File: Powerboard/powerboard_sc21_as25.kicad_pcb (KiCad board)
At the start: 2 copper layers, 86.2 x 40 mm, 117 parts, among them IC1 BQ24618RGET-iclr, IC2 CP2102, Q1 SI7617DN-T1-GE3, Q10 CSD25302Q2, Q2 SI7617DN-T1-GE3, Q3 SI7617DN-T1-GE3, Q6 MMDT2222A, Q7 SI7617DN-T1-GE3, Q8 SI7617DN-T1-GE3, Q9 CSD25302Q2, U1 LTC4412xS6, U10 RT9025-25GSP, U11 LTC4411, U2 ESP32-PICO-D4, U3 SN65HVD230, U4 LTC4412xS6, U5 LTC4412xS6, U6 LM2679T-3.3-iclr, U7 LM2679T-3.3-iclr, U8 LTC4412xS6, U9 LTC4412xS6

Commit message: changed some FP assignments and imported components
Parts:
- removed ANT1: AMCA31-2R450G-S1F-T3, iclr:ANT_AMCA31-2R450G-S1F-T3
- removed R25: 3.5k, Resistor_SMD:R_0603_1608Metric
- removed R33: 24k, Resistor_SMD:R_0603_1608Metric
- removed R34: 47k, Resistor_SMD:R_0603_1608Metric
- removed REF** (x2): AMASS_XT60-M, AMASS_XT60-M
- removed REF** (x4): MountingHole_3.2mm_M3_DIN965_Pad, MountingHole:MountingHole_3.2mm_M3_DIN965_Pad
- removed REF**: USB_C_Receptacle_GCT_USB4085, Connector_USB:USB_C_Receptacle_GCT_USB4085
- removed REF**: Molex_Mini-Fit_Jr_5566-08A_2x04_P4.20mm_Vertical, Connector_Molex:Molex_Mini-Fit_Jr_5566-08A_2x04_P4.20mm_Vertical
- removed REF**: Molex_Mini-Fit_Jr_5566-04A_2x02_P4.20mm_Vertical, Connector_Molex:Molex_Mini-Fit_Jr_5566-04A_2x02_P4.20mm_Vertical
- removed U4, U5: LTC4412xS6, Package_TO_SOT_SMD:TSOT-23-6
- added C26: 0.1uF, Capacitor_SMD:C_0603_1608Metric, F.Cu at (229.3, 118.8)
- added C27: 220pF, Capacitor_SMD:C_0603_1608Metric, F.Cu at (233.3, 119.9)
- added C28: 220 pF, Capacitor_SMD:C_0603_1608Metric, F.Cu at (266.8, 84.4)
- added C29: 15uF, Capacitor_SMD:CP_Elec_5x5.3, F.Cu at (240.5, 62.0)
- added C30: 15uF, Capacitor_SMD:CP_Elec_5x5.3, F.Cu at (260.4, 56.0)
- added C31: 0.1μF, Capacitor_SMD:C_0603_1608Metric, F.Cu at (330.1, 51.2)
- added C32: 22μF, Capacitor_SMD:C_1210_3225Metric, F.Cu at (282.3, 73.2)
- added C33: 0.1μF, Capacitor_SMD:C_0603_1608Metric, F.Cu at (334.6, 44.8)
- added C36: 0.01uF, Capacitor_SMD:C_0603_1608Metric, F.Cu at (263.6, 41.4)
- added C37: 0.01uF, Capacitor_SMD:C_0603_1608Metric, F.Cu at (226.8, 76.9)
- added C38: 330uF, Capacitor_SMD:CP_Elec_10x10, F.Cu at (243.3, 39.2)
- added C39: 330uF, Capacitor_SMD:CP_Elec_10x10, F.Cu at (215.2, 37.0)
- added C51: 0.1muF, Capacitor_SMD:C_0603_1608Metric, F.Cu at (288.8, 100.2)
- added C52: 4.7muF, Capacitor_SMD:C_0603_1608Metric, F.Cu at (293.2, 97.0)
- added C53: 0.1muF, Capacitor_SMD:C_0603_1608Metric, F.Cu at (302.6, 87.4)
- added C54: 10uF, Capacitor_SMD:C_0805_2012Metric, F.Cu at (298.8, 84.7)
- added C57: 10uF, Capacitor_SMD:C_0805_2012Metric, F.Cu at (291.4, 91.8)
- added C58: 4.7uF, Capacitor_SMD:C_0603_1608Metric, F.Cu at (284.7, 102.1)
- added D1: BAT54, Diode_SMD:D_SOT-23_ANK, F.Cu at (344.0, 35.6)
- added D4: SM712_SOT23, Package_TO_SOT_SMD:SOT-23, F.Cu at (222.2, 123.7)
- added D5: DST1550S, Package_TO_SOT_SMD:TO-277B, F.Cu at (250.3, 58.0)
- added D8: SP0503BAHT, Package_TO_SOT_SMD:SOT-143, F.Cu at (288.6, 96.7)
- added H1: MountingHole_Pad, MountingHole:MountingHole_3.2mm_M3_DIN965_Pad, F.Cu at (210.6, 122.4)
- added H2: MountingHole_Pad, MountingHole:MountingHole_3.2mm_M3_DIN965_Pad, F.Cu at (261.2, 86.8)
- added H3: MountingHole_Pad, MountingHole:MountingHole_3.2mm_M3_DIN965_Pad, F.Cu at (233.4, 110.0)
- added H4: MountingHole_Pad, MountingHole:MountingHole_3.2mm_M3_DIN965_Pad, F.Cu at (217.7, 117.8)
- added J1: Thermistor Connection 103AT NTC, Connector_JST:JST_XH_B2B-XH-AM_1x02_P2.50mm_Vertical, F.Cu at (318.2, 49.0)
- added J10: Conn_01x04_Male, Connector_JST:JST_XH_B4B-XH-AM_1x04_P2.50mm_Vertical, F.Cu at (214.2, 109.8)
- added J2: Conn_01x02_Male, Connector_PinHeader_2.54mm:PinHeader_1x02_P2.54mm_Vertical, F.Cu at (227.5, 108.8)
- added J3: Conn_01x02_Male, Connector_PinHeader_2.54mm:PinHeader_1x02_P2.54mm_Vertical, F.Cu at (204.7, 121.2)
- added J4: Conn_01x08_Male, Connector_Molex:Molex_Mini-Fit_Jr_5566-08A_2x04_P4.20mm_Vertical, F.Cu at (305.5, 131.1)
- added J5: Conn_01x04_Male, Connector_Molex:Molex_Mini-Fit_Jr_5566-04A_2x02_P4.20mm_Vertical, F.Cu at (351.0, 121.3)
- added J6: Conn_01x02_Male, Connector_AMASS:AMASS_XT60-M_1x02_P7.20mm_Vertical, F.Cu at (302.3, 51.5)
- added J7: IsolationSwitch, Connector_AMASS:AMASS_XT60-M_1x02_P7.20mm_Vertical, F.Cu at (329.4, 38.4)
- added J8: USB_C_Receptacle_USB2.0, Connector_USB:USB_C_Receptacle_GCT_USB4085, F.Cu at (280.4, 84.8)
- added J9: Conn_Coaxial, Connector_Coaxial:U.FL_Molex_MCRF_73412-0110_Vertical, F.Cu at (224.3, 117.3)
- added JP1: SolderJumper_2_Open, Jumper:SolderJumper-2_P1.3mm_Open_RoundedPad1.0x1.5mm, F.Cu at (216.9, 123.2)
- added L1: 6.8µH, iclr:INDM8681X400N, F.Cu at (304.7, 61.5)
- added L3: 15uH, Inductor_SMD:L_12x12mm_H8mm, F.Cu at (200.5, 54.7)
- added L4: 15uH, Inductor_SMD:L_12x12mm_H8mm, F.Cu at (200.5, 40.4)
- added Q4: RS1G120MN, Package_SO:HSOP-8-1EP_3.9x4.9mm_P1.27mm_EP2.41x3.1mm, F.Cu at (328.4, 46.8)
- added Q5: RS1G120MN, Package_SO:HSOP-8-1EP_3.9x4.9mm_P1.27mm_EP2.41x3.1mm, F.Cu at (314.3, 59.8)
- added R39: 47k, Resistor_SMD:R_0603_1608Metric, F.Cu at (293.2, 94.5)
- added R40: 4.7k, Resistor_SMD:R_0603_1608Metric, F.Cu at (297.2, 96.5)
- added R42: 56k, Resistor_SMD:R_0603_1608Metric, F.Cu at (297.2, 94.0)
- added R43: 10k, Resistor_SMD:R_0603_1608Metric, F.Cu at (295.6, 91.5)
- added RAdp1: 150kΩ, Resistor_SMD:R_0603_1608Metric, F.Cu at (334.6, 49.8)
- added RFast1: 32kΩ, Resistor_SMD:R_0603_1608Metric, F.Cu at (348.2, 37.0)
- added RPre1: 13kΩ, Resistor_SMD:R_0603_1608Metric, F.Cu at (313.9, 69.8)
- added TP1: TestPoint, TestPoint:TestPoint_Pad_D1.0mm, F.Cu at (242.6, 113.0)
- added TP10: TestPoint, TestPoint:TestPoint_Pad_D1.0mm, F.Cu at (263.1, 94.9)
- added TP11: TestPoint, TestPoint:TestPoint_Pad_D1.0mm, F.Cu at (266.3, 87.2)
- added TP12: TestPoint, TestPoint:TestPoint_Pad_D1.0mm, F.Cu at (246.6, 108.5)
- added TP13: TestPoint, TestPoint:TestPoint_Pad_D1.0mm, F.Cu at (257.9, 100.1)
- added TP14: TestPoint, TestPoint:TestPoint_Pad_D1.0mm, F.Cu at (257.9, 97.0)
- added TP15: TestPoint, TestPoint:TestPoint_Pad_D1.0mm, F.Cu at (230.2, 122.7)
- added TP16: TestPoint, TestPoint:TestPoint_Pad_D1.0mm, F.Cu at (328.1, 59.0)
- added TP17: TestPoint, TestPoint:TestPoint_Pad_D1.0mm, F.Cu at (351.7, 37.3)
- added TP18: TestPoint, TestPoint:TestPoint_Pad_D1.0mm, F.Cu at (338.2, 50.1)
- added TP19: TestPoint, TestPoint:TestPoint_Pad_D1.0mm, F.Cu at (235.5, 75.8)
- added TP2: TestPoint, TestPoint:TestPoint_Pad_D1.0mm, F.Cu at (270.3, 84.7)
- added TP20: TestPoint, TestPoint:TestPoint_Pad_D1.0mm, F.Cu at (272.1, 34.8)
- added TP21: TestPoint, TestPoint:TestPoint_Pad_D1.0mm, F.Cu at (262.1, 48.2)
- added TP22: TestPoint, TestPoint:TestPoint_Pad_D1.0mm, F.Cu at (272.1, 37.9)
- added TP23: TestPoint, TestPoint:TestPoint_Pad_D1.0mm, F.Cu at (303.2, 90.2)
- added TP24: TestPoint, TestPoint:TestPoint_Pad_D1.0mm, F.Cu at (310.5, 84.7)
- added TP25: TestPoint, TestPoint:TestPoint_Pad_D1.0mm, F.Cu at (292.7, 99.8)
- added TP26: TestPoint, TestPoint:TestPoint_Pad_D1.0mm, F.Cu at (233.2, 122.7)
- added TP27: TestPoint, TestPoint:TestPoint_Pad_D1.0mm, F.Cu at (230.2, 125.7)
- added TP3: TestPoint, TestPoint:TestPoint_Pad_D1.0mm, F.Cu at (266.3, 90.3)
- added TP4: TestPoint, TestPoint:TestPoint_Pad_D1.0mm, F.Cu at (250.6, 102.1)
- added TP5: TestPoint, TestPoint:TestPoint_Pad_D1.0mm, F.Cu at (253.7, 102.1)
- added TP6: TestPoint, TestPoint:TestPoint_Pad_D1.0mm, F.Cu at (250.6, 105.1)
- added TP7: TestPoint, TestPoint:TestPoint_Pad_D1.0mm, F.Cu at (212.3, 115.8)
- added TP8: TestPoint, TestPoint:TestPoint_Pad_D1.0mm, F.Cu at (263.1, 91.8)
- added TP9: TestPoint, TestPoint:TestPoint_Pad_D1.0mm, F.Cu at (237.1, 117.7)
- C12, C13, C8, C9: value 10μF -> 10uF; footprint Capacitor_SMD:C_0603_1608Metric -> Capacitor_SMD:C_0805_2012Metric
- C16: value 2.2μF -> 2.2uF; footprint Capacitor_SMD:C_0603_1608Metric -> Capacitor_SMD:C_0805_2012Metric
- C19: value 1.2pF -> 15uF; footprint Capacitor_SMD:C_0603_1608Metric -> Capacitor_SMD:CP_Elec_5x5.3
- C20: value 1.5pF -> 15uF; footprint Capacitor_SMD:C_0603_1608Metric -> Capacitor_SMD:CP_Elec_5x5.3
- C21: value C_Small -> 160pF
- C22: value C_Small -> 10uF; footprint Capacitor_SMD:C_0603_1608Metric -> Capacitor_SMD:C_0805_2012Metric
- C23: value CP -> 100nF
- C24: value CP -> 0.1uF
- C25: value 0.1μF -> 10uF
- C34: value C_Small -> 15uF; footprint Capacitor_SMD:C_0603_1608Metric -> Capacitor_SMD:CP_Elec_5x5.3
- C35: value 0.47μF -> 15uF; footprint Capacitor_SMD:C_0603_1608Metric -> Capacitor_SMD:CP_Elec_5x5.3
- C40, C41: value 0.1µF -> 330uF; footprint Capacitor_SMD:C_0603_1608Metric -> Capacitor_SMD:CP_Elec_10x10
- C42: value 1.0muF -> 0.47uF; footprint Capacitor_SMD:C_0603_1608Metric -> Capacitor_SMD:C_0805_2012Metric
- C43: value 0.1muF -> 0.47μF; footprint Capacitor_SMD:C_0603_1608Metric -> Capacitor_SMD:C_0805_2012Metric
- C44: value 4.7muF -> 330uF; footprint Capacitor_SMD:C_0603_1608Metric -> Capacitor_SMD:CP_Elec_10x10
- C45: value 0.1muF -> 330uF; footprint Capacitor_SMD:C_0603_1608Metric -> Capacitor_SMD:CP_Elec_10x10
- C46: value 10uF -> 330uF; footprint Capacitor_SMD:C_0603_1608Metric -> Capacitor_SMD:CP_Elec_10x10
- C47: value 1uF -> 330uF; footprint Capacitor_SMD:C_0603_1608Metric -> Capacitor_SMD:CP_Elec_10x10
- C48: value 0.1uF -> 0.1µF
- C49: value 10uF -> 0.1µF
- C5: value 1μF -> 1uF
- C50: value 4.7uF -> 1.0muF
- C7: value 1µF -> 1uF
- D6: value LED -> DST1550S; footprint LED_SMD:LED_0603_1608Metric -> Package_TO_SOT_SMD:TO-277B
- D7: value SP0503BAHT -> LED; footprint Package_TO_SOT_SMD:SOT-143 -> LED_SMD:LED_0603_1608Metric
- IC1: footprint Package_DFN_QFN:VQFN-24-1EP_4x4mm_P0.5mm_EP2.45x2.45mm_ThermalVias -> Package_DFN_QFN:VQFN-24-1EP_4x4mm_P0.5mm_EP2.45x2.45mm
- IC2: footprint Package_DFN_QFN:QFN-28-1EP_4x4mm_P0.4mm_EP2.4x2.4mm -> iclr:QFN28G_0.5-5X5MM
- Q1, Q2, Q3, Q7, Q8: value SI7617DN-T1-GE3 -> RSJ250P10TL; footprint iclr:SIS862DNT1GE3 -> Package_TO_SOT_SMD:TO-263-3_TabPin2
- Q10, Q9: value CSD25302Q2 -> MCH6351; footprint Package_SON:Texas_DQK -> Package_TO_SOT_SMD:SOT-363_SC-70-6
- R12, R13, R24: value 470Ω -> 10k
- R19: value 10kΩ -> 470Ω
- R21: value 10k -> 470Ω
- R22: value 10k -> 120
- R23: value 470Ω -> 120
- R26: value 3.5k -> 60
- R27: value 1kΩ -> 60
- R28, R29: value R_Small -> 3.5k
- R30: value 5.1k -> 75k
- R31: value 5.1k -> 10k
- R32: value 470Ω -> 1kΩ
- R35: value 4.7k -> 5.1k
- R36: value 100k -> 5.1k
- R37: value 147k -> 470Ω
- R38: value 47k -> 24k
- R4: value 150kΩ -> 10kΩ
- R6: value 13kΩ -> 470Ω
- R8: value 32kΩ -> 470Ω
- RAC1, RSR1: footprint Capacitor_SMD:C_0603_1608Metric -> Resistor_SMD:R_0603_1608Metric
- U2: value ESP32-PICO-D4 -> SN65HVD230; footprint Package_DFN_QFN:QFN-48-1EP_7x7mm_P0.5mm_EP5.3x5.3mm -> Package_SO:SOIC-8_3.9x4.9mm_P1.27mm
- U3: value SN65HVD230 -> ESP32-PICO-D4; footprint Package_SO:SOIC-8_3.9x4.9mm_P1.27mm -> Package_DFN_QFN:QFN-48-1EP_7x7mm_P0.5mm_EP5.3x5.3mm
- U6, U7: footprint Package_TO_SOT_SMD:TO-263-7_TabPin8 -> Package_TO_SOT_SMD:TO-263-7_TabPin4
- moved C5 321.2 mm to (342.7, 44.8)
- moved C7 319.6 mm to (338.6, 44.8)
- moved C14 313.0 mm to (338.6, 47.3)
- moved C10 307.2 mm to (326.1, 51.2)
- moved C11 306.5 mm to (347.8, 39.6)
- moved C4 295.6 mm to (320.5, 64.7)
- moved C15 295.2 mm to (320.7, 54.7)
- moved C1 294.6 mm to (316.5, 66.8)
- moved C6 290.5 mm to (324.5, 57.2)
- moved C3 287.7 mm to (313.4, 72.3)
- moved C9 285.2 mm to (305.6, 67.9)
- moved C50 275.7 mm to (303.0, 84.4)
- moved R37 275.5 mm to (307.0, 84.4)
- moved C13 275.1 mm to (296.2, 74.2)
- moved C8 274.8 mm to (312.3, 64.5)
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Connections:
- C12 pad 1: /Battery Charger/Q3-S -> GND
- C12 pad 2: GND -> /Battery Charger/Q3-S
- C13 pad 1: /Battery Charger/Q3-S -> GND
- C13 pad 2: GND -> /Battery Charger/Q3-S
- C15 pad 1: /Battery Charger/Q4-D -> +24V
- C16 pad 1: Net-(C16-Pad1) -> GND
- C16 pad 2: GND -> Net-(C16-Pad2)
- C19 pad 1: /LNA_IN -> +24V
- C20 pad 1: Net-(ANT1-Pad1) -> +24V
- C21 pad 1: +3V3 -> GND
- C21 pad 2: GND -> Net-(C21-Pad2)
- C23 pad 1: GND -> +3V3
- C23 pad 2: Net-(GroundPower1-Pad1) -> GND
- C24 pad 1: GND -> +3V3
- C24 pad 2: Net-(C24-Pad2) -> GND
- C25 pad 1: GND -> +3V3
- C25 pad 2: Net-(C3-Pad1) -> GND
- C3 pad 2: /Battery Charger/Q4-D -> +24V
- C40 pad 1: Net-(C37-Pad1) -> Net-(C38-Pad1)
- C40 pad 2: GND -> Net-(C38-Pad2)
- C41 pad 1: Net-(C36-Pad1) -> Net-(C37-Pad2)
- C41 pad 2: GND -> Net-(C41-Pad2)
- C42 pad 1: +3V3 -> +24V
- C43 pad 1: +3V3 -> +24V
- C44 pad 1: GND -> Net-(C38-Pad1)
- C44 pad 2: +3V3 -> Net-(C38-Pad2)
- C45 pad 1: GND -> Net-(C37-Pad2)
- C45 pad 2: +3V3 -> Net-(C41-Pad2)
- C46 pad 1: GND -> Net-(C37-Pad2)
- C46 pad 2: VBUS -> Net-(C41-Pad2)
- C47 pad 1: GND -> Net-(C37-Pad2)
- C47 pad 2: VBUS -> Net-(C41-Pad2)
- C48 pad 1: Net-(C48-Pad1) -> Net-(C37-Pad2)
- C48 pad 2: Net-(C48-Pad2) -> GND
- C49 pad 1: GND -> Net-(C38-Pad1)
- C49 pad 2: Net-(C48-Pad2) -> GND
- C7 pad 1: /Battery Charger/VCC -> GND
- C7 pad 2: GND -> /Battery Charger/VCC
- C8 pad 1: /Battery Charger/Q4-D -> GND
- C8 pad 2: GND -> +24V
- C9 pad 1: /Battery Charger/Q4-D -> GND
- C9 pad 2: GND -> +24V
- CTTC1 pad 1: Net-(CTTC1-Pad1) -> GND
- CTTC1 pad 2: GND -> Net-(CTTC1-Pad2)
- D6 pad 1: GND -> Net-(C38-Pad2)
- D6 pad 2: Net-(D6-Pad2) -> GND
- D7 pad 2: VBUS -> Net-(D7-Pad2)
- IC1 pad 1: /Battery Charger/Q4-D -> +24V
- IC1 pad 11: Net-(R7-Pad2) -> Net-(IC1-Pad11)
- IC1 pad 25: unconnected-(IC1-Pad25) -> GND
- IC1 pad 7: Net-(CTTC1-Pad1) -> Net-(CTTC1-Pad2)
- IC2 pad 4: Net-(D7-Pad4) -> Net-(D8-Pad4)
- IC2 pad 5: Net-(D7-Pad3) -> Net-(D8-Pad3)
- Q1 pad 1: Net-(PowerLED1-Pad2) -> /Battery Charger/Q1-G
- Q1 pad 2: Net-(PowerLED1-Pad2) -> /Battery Charger/Q1-D
- Q10 pad 1: Net-(C24-Pad2) -> +3V3
- Q10 pad 2: Net-(C24-Pad2) -> +3V3
- Q10 pad 4: /Battery Charger/Q3-S -> Net-(C37-Pad2)
- Q10 pad 5: Net-(C24-Pad2) -> +3V3
- Q10 pad 6: Net-(C24-Pad2) -> +3V3
- Q2 pad 1: Net-(C3-Pad1) -> /Battery Charger/Q1-G
- Q2 pad 2: Net-(C3-Pad1) -> /Battery Charger/Q1-D
- Q3 pad 1: /Battery Charger/Q3-S -> Net-(C15-Pad2)
- Q3 pad 2: /Battery Charger/Q3-S -> +24V
- Q7 pad 1: Net-(J4-Pad3) -> Net-(Q7-Pad1)
- Q7 pad 2: Net-(J4-Pad3) -> Net-(Q7-Pad2)
- Q7 pad 3: Net-(J4-Pad3) -> Net-(J4-Pad4)
- Q8 pad 1: +24V -> Net-(Q7-Pad1)
- Q8 pad 2: +24V -> Net-(Q7-Pad2)
- Q9 pad 1: Net-(GroundPower1-Pad1) -> +3V3
- Q9 pad 2: Net-(GroundPower1-Pad1) -> +3V3
- Q9 pad 4: Net-(PowerLED1-Pad2) -> Net-(C38-Pad1)
- Q9 pad 5: Net-(GroundPower1-Pad1) -> +3V3
- Q9 pad 6: Net-(GroundPower1-Pad1) -> +3V3
- R11 pad 2: /EN -> /BOOT
- R12 pad 1: Net-(C17-Pad2) -> Net-(Q6-Pad2)
- R12 pad 2: /EN -> /DTR
- R13 pad 1: Net-(C18-Pad2) -> Net-(Q6-Pad5)
- R13 pad 2: /BOOT -> /RTS
- R15 pad 2: /Battery Charger/Q4-D -> +24V
- R19 pad 1: +3V3 -> Net-(D2-Pad2)
- R19 pad 2: /BOOT -> +3V3
- R20 pad 1: Net-(C16-Pad1) -> Net-(C16-Pad2)
- R21 pad 1: Net-(Q6-Pad2) -> Net-(D3-Pad2)
- R21 pad 2: /DTR -> +3V3
- R22 pad 1: Net-(Q6-Pad5) -> /CAN_TX
- R22 pad 2: /RTS -> Net-(C21-Pad2)
- R23 pad 1: Net-(D2-Pad2) -> /CAN_RX
- R23 pad 2: +3V3 -> Net-(R23-Pad2)
- R24 pad 1: Net-(D3-Pad2) -> Net-(R24-Pad1)
- R24 pad 2: +3V3 -> GND
- R26 pad 1: Net-(PowerLED1-Pad1) -> /CANH
- R26 pad 2: GND -> Net-(C26-Pad1)
- R27 pad 1: Net-(IC1-Pad23) -> Net-(C26-Pad1)
- R27 pad 2: Net-(C15-Pad2) -> /CANL
- R28 pad 1: Net-(R28-Pad1) -> Net-(PackLED1-Pad1)
- R29 pad 1: Net-(R29-Pad1) -> Net-(PowerLED1-Pad1)
- R30 pad 1: GND -> Net-(C31-Pad1)
- R30 pad 2: Net-(J6-PadA5) -> /CHARGE
- R31 pad 1: GND -> /CHARGE
- R31 pad 2: Net-(J6-PadB5) -> GND
- R32 pad 1: VBUS -> Net-(IC1-Pad23)
- R32 pad 2: Net-(D6-Pad2) -> Net-(C15-Pad2)
- R35 pad 1: +3V3 -> GND
- R35 pad 2: Net-(IC2-Pad9) -> Net-(J8-PadA5)
- R36 pad 1: Net-(R36-Pad1) -> GND
- R36 pad 2: GND -> Net-(J8-PadB5)
- R37 pad 1: Net-(C48-Pad2) -> VBUS
- R37 pad 2: Net-(C48-Pad1) -> Net-(D7-Pad2)
- R38 pad 1: Net-(C48-Pad1) -> VBUS
- R38 pad 2: GND -> Net-(IC2-Pad8)
- R4 pad 1: /Battery Charger/ACSET -> +3V3
- R4 pad 2: GND -> /EN
- R6 pad 1: /Battery Charger/ISET2 -> Net-(C17-Pad2)
- R6 pad 2: GND -> /EN
- R7 pad 2: Net-(R7-Pad2) -> Net-(IC1-Pad11)
- R8 pad 1: Net-(R7-Pad2) -> Net-(C18-Pad2)
- R8 pad 2: GND -> /BOOT
- RAC1 pad 1: /Battery Charger/Q4-D -> +24V
- U1 pad 5: Net-(Q7-Pad4) -> Net-(Q7-Pad1)
- U1 pad 6: Net-(J4-Pad3) -> Net-(J4-Pad4)
- U10 pad 1: Net-(R36-Pad1) -> unconnected-(U10-Pad1)
- U10 pad 4: VBUS -> unconnected-(U10-Pad4)
- U10 pad 6: Net-(C48-Pad2) -> Net-(C57-Pad2)
- U10 pad 7: Net-(C48-Pad1) -> Net-(R42-Pad2)
- U11 pad 1: Net-(C48-Pad2) -> Net-(C57-Pad2)
- U2 pad 1: +3V3 -> Net-(C21-Pad2)
- U2 pad 2: /LNA_IN -> GND
- U2 pad 4: +3V3 -> Net-(R23-Pad2)
- U2 pad 5: unconnected-(U2-Pad5) -> /Vref
- U2 pad 6: unconnected-(U2-Pad6) -> /CANL
- U2 pad 7: unconnected-(U2-Pad7) -> /CANH
- U2 pad 8: unconnected-(U2-Pad8) -> Net-(R24-Pad1)
- U3 pad 1: /CAN_TX -> +3V3
- U3 pad 2: GND -> /LNA_IN
- U3 pad 4: /CAN_RX -> +3V3
- U3 pad 6: /CANL -> unconnected-(U3-Pad6)
- U3 pad 7: /CANH -> unconnected-(U3-Pad7)
- U3 pad 8: GND -> unconnected-(U3-Pad8)
- U6 pad 1: Net-(D4-Pad4) -> Net-(C36-Pad2)
- U6 pad 3: unconnected-(U6-Pad3) -> Net-(C36-Pad1)
- U6 pad 5: Net-(R28-Pad1) -> unconnected-(U6-Pad5)
- U6 pad 6: Net-(C36-Pad1) -> Net-(C38-Pad1)
- U7 pad 1: Net-(D5-Pad4) -> Net-(C37-Pad2)
- U7 pad 3: unconnected-(U7-Pad3) -> Net-(C37-Pad1)
- U7 pad 5: Net-(R29-Pad1) -> unconnected-(U7-Pad5)
- U7 pad 6: Net-(C37-Pad1) -> Net-(C37-Pad2)
- U8 pad 1: Net-(C37-Pad1) -> Net-(C37-Pad2)
- U8 pad 5: Net-(Q12-Pad1) -> Net-(Q10-Pad3)
- U9 pad 1: Net-(C36-Pad1) -> Net-(C38-Pad1)
- U9 pad 5: Net-(Q11-Pad1) -> Net-(Q9-Pad3)
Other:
- copper layers 2 -> 4

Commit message: grouped components by circuit, done CAN transceiver layout.
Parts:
- removed U10: RT9025-25GSP, Package_SO:SOP-8_3.9x4.9mm_P1.27mm
- added U4: RT9025-25GSP, iclr:SOIC127P599X175-9N, F.Cu at (530.6, -45.9)
- C25: footprint Capacitor_SMD:C_0603_1608Metric -> Capacitor_SMD:C_0805_2012Metric
- moved U7 374.9 mm to (-71.1, 210.6)
- moved C20 359.8 mm to (-32.5, 237.4)
- moved C30 359.8 mm to (-38.2, 256.6)
- moved C35 359.8 mm to (-78.0, 272.9)
- moved D5 348.8 mm to (-43.2, 246.4)
- moved C36 347.7 mm to (-83.0, 14.0), turned to 180 degrees
- moved C41 346.9 mm to (-80.5, 244.3)
- moved C45 346.9 mm to (-66.4, 244.3)
- moved C47 346.9 mm to (-80.5, 232.5)
- moved C46 346.9 mm to (-95.3, 249.1)
- moved C38 344.4 mm to (-94.4, -28.6)
- moved C43 344.3 mm to (-106.7, 212.1)
- moved C34 336.6 mm to (-99.2, -0.05)
- moved C29 328.9 mm to (-82.1, -1.99)
- moved U6 319.4 mm to (-72.2, 16.4)
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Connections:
- TP25 pad 1: unconnected-(TP25-Pad1) -> GND
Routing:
- net GND: vias 0 -> 1
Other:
- board size 86.2 x 40 mm -> 86 x 40 mm

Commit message: Tuesday's changes (I don't remember what I did)
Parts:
- moved J7 702.0 mm to (290.9, 725.3)
- moved PackLED1 543.5 mm to (705.1, 439.1)
- moved L1 542.9 mm to (622.2, 498.7)
- moved R28 540.3 mm to (705.8, 441.0)
- moved C13 539.8 mm to (547.4, 552.0)
- moved C12 528.2 mm to (573.9, 519.1)
- moved Q4 514.9 mm to (323.5, 553.2)
- moved Q3 514.1 mm to (358.6, 549.7)
- moved Q5 494.0 mm to (331.7, 553.5)
- moved RSR1 490.6 mm to (585.4, 475.7)
- moved C15 487.4 mm to (351.9, 541.1)
- moved J6 486.7 mm to (607.7, 406.9)
- moved R15 481.1 mm to (352.2, 534.5)
- moved C6 478.8 mm to (539.6, 485.0)
- moved R32 470.2 mm to (354.3, 526.2)
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
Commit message: Finalised buck capacitors, some inital layout
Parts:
- removed C29, C30, C34, C35: 15uF, Capacitor_SMD:CP_Elec_5x5.3
- removed C46, C47: 330uF, Capacitor_SMD:CP_Elec_10x10
- C19, C20: value 15uF -> 47uF; footprint Capacitor_SMD:CP_Elec_5x5.3 -> Capacitor_SMD:C_2220_5650Metric
- C38, C39, C40, C41: footprint Capacitor_SMD:CP_Elec_10x10 -> Capacitor_Tantalum_SMD:CP_EIA-7343-30_AVX-N
- C44, C45: value 330uF -> 22uF; footprint Capacitor_SMD:CP_Elec_10x10 -> Capacitor_SMD:C_0603_1608Metric
- moved C45 300.5 mm to (35.0, -38.6)
- moved C41 242.6 mm to (73.1, 56.5), turned to -90 degrees
- moved C39 179.1 mm to (77.9, 56.5), turned to -90 degrees
- moved C36 172.6 mm to (78.5, 75.0)
- moved C19 160.5 mm to (74.4, 63.9)
- moved C42 155.9 mm to (74.0, 67.9)
- moved U6 148.1 mm to (64.2, 74.2), turned to -90 degrees
- moved L3 121.5 mm to (64.1, 59.0), turned to 90 degrees
- moved C49 116.5 mm to (101.1, -24.0), turned to -90 degrees
- moved C38 114.4 mm to (13.3, 9.83)
- moved Q9 113.3 mm to (107.4, -23.9), turned to 90 degrees
- moved D6 108.2 mm to (49.3, 64.8), turned to 180 degrees
- moved U9 105.4 mm to (103.9, -23.8)
- moved C40 75.2 mm to (12.2, 3.73)
- moved C44 75.2 mm to (27.7, 1.44)
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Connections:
- C38 pad 1: Net-(C38-Pad1) -> Net-(C37-Pad2)
- C38 pad 2: Net-(C38-Pad2) -> GND
- C39 pad 1: Net-(C38-Pad1) -> Net-(C49-Pad1)
- C39 pad 2: Net-(C38-Pad2) -> GND
- C40 pad 1: Net-(C38-Pad1) -> Net-(C37-Pad2)
- C40 pad 2: Net-(C38-Pad2) -> GND
- C41 pad 1: Net-(C37-Pad2) -> Net-(C49-Pad1)
- C41 pad 2: Net-(C41-Pad2) -> GND
- C44 pad 1: Net-(C38-Pad1) -> Net-(C37-Pad2)
- C44 pad 2: Net-(C38-Pad2) -> GND
- C45 pad 1: Net-(C37-Pad2) -> Net-(C49-Pad1)
- C45 pad 2: Net-(C41-Pad2) -> GND
- C49 pad 1: Net-(C38-Pad1) -> Net-(C49-Pad1)
- D5 pad 1: Net-(C41-Pad2) -> GND
- D6 pad 1: Net-(C38-Pad2) -> GND
- L3 pad 2: Net-(C38-Pad1) -> Net-(C49-Pad1)
- Q9 pad 4: Net-(C38-Pad1) -> Net-(C49-Pad1)
- U6 pad 6: Net-(C38-Pad1) -> Net-(C49-Pad1)
- U9 pad 1: Net-(C38-Pad1) -> Net-(C49-Pad1)
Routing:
- net Net-(C36-Pad1): track 0.00 -> 1.30 mm
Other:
- board size 86 x 40 mm -> 86 x 41 mm

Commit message: moving around charger components
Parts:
- moved TP17 506.0 mm to (598.4, 479.1)
- moved TP16 500.4 mm to (575.0, 494.2)
- moved J7 384.0 mm to (585.1, 478.6)
- moved RPre1 339.1 mm to (600.1, 521.1), turned to -90 degrees
- moved Q4 294.0 mm to (613.0, 502.5)
- moved R5 287.1 mm to (600.1, 518.2), turned to -90 degrees
- moved Q5 287.0 mm to (613.1, 497.1), turned to 180 degrees
- moved C9 280.5 mm to (619.8, 499.8), turned to -90 degrees
- moved R3 278.6 mm to (601.5, 518.2), turned to -90 degrees
- moved RAdp1 277.7 mm to (601.5, 521.1), turned to -90 degrees
- moved C8 275.4 mm to (617.8, 499.8), turned to -90 degrees
- moved R7 260.9 mm to (598.6, 518.2), turned to -90 degrees
- moved C10 256.8 mm to (606.1, 516.5), turned to 90 degrees
- moved C14 255.4 mm to (579.8, 515.8), turned to -90 degrees
- moved R17 255.0 mm to (583.5, 515.0), turned to 180 degrees
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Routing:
- net Net-(C36-Pad1): track 1.30 -> 0.00 mm
- net +24V: track 0.00 -> 1.30 mm

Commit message: layout
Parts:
- C21, C23, C25, C26, C27, C28, C50, C51, C52, C53, C54, C57, C58, D2, D3, D4, D7, D8, J8, JP1, Q6, R12, R13, R19, R21, R22, R23, R24, R26, R27, R35, R36, R37, R38, R39, R40, R42, R43, TP14, TP15, TP23, TP25, U11, U2: moved to B.Cu
- moved C7 700.8 mm to (75.8, 31.1), turned to 0 degrees
- moved R17 698.9 mm to (78.0, 32.4), turned to -90 degrees
- moved R18 698.9 mm to (79.5, 32.4), turned to 90 degrees
- moved C16 698.3 mm to (75.6, 32.9), turned to 0 degrees
- moved J1 694.4 mm to (84.6, 33.8), turned to 90 degrees
- moved R14 692.1 mm to (80.2, 38.3), turned to 90 degrees
- moved R29 691.7 mm to (78.0, 35.4), turned to -90 degrees
- moved PowerLED1 691.7 mm to (79.5, 35.4), turned to -90 degrees
- moved R20 691.6 mm to (81.0, 35.4), turned to -90 degrees
- moved C14 689.9 mm to (82.5, 37.6), turned to 180 degrees
- moved D1 686.4 mm to (101.6, 41.4), turned to 180 degrees
- moved Q1 685.7 mm to (73.8, 42.2), turned to -90 degrees
- moved C5 684.9 mm to (103.3, 43.9)
- moved IC1 683.9 mm to (98.3, 45.8)
- moved R9 683.8 mm to (92.2, 49.3)
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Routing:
- net GND: track 0.00 -> 1.30 mm, vias 1 -> 0
- net +24V: track 1.30 -> 0.00 mm
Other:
- board size 86 x 41 mm -> 86.1 x 55.6 mm

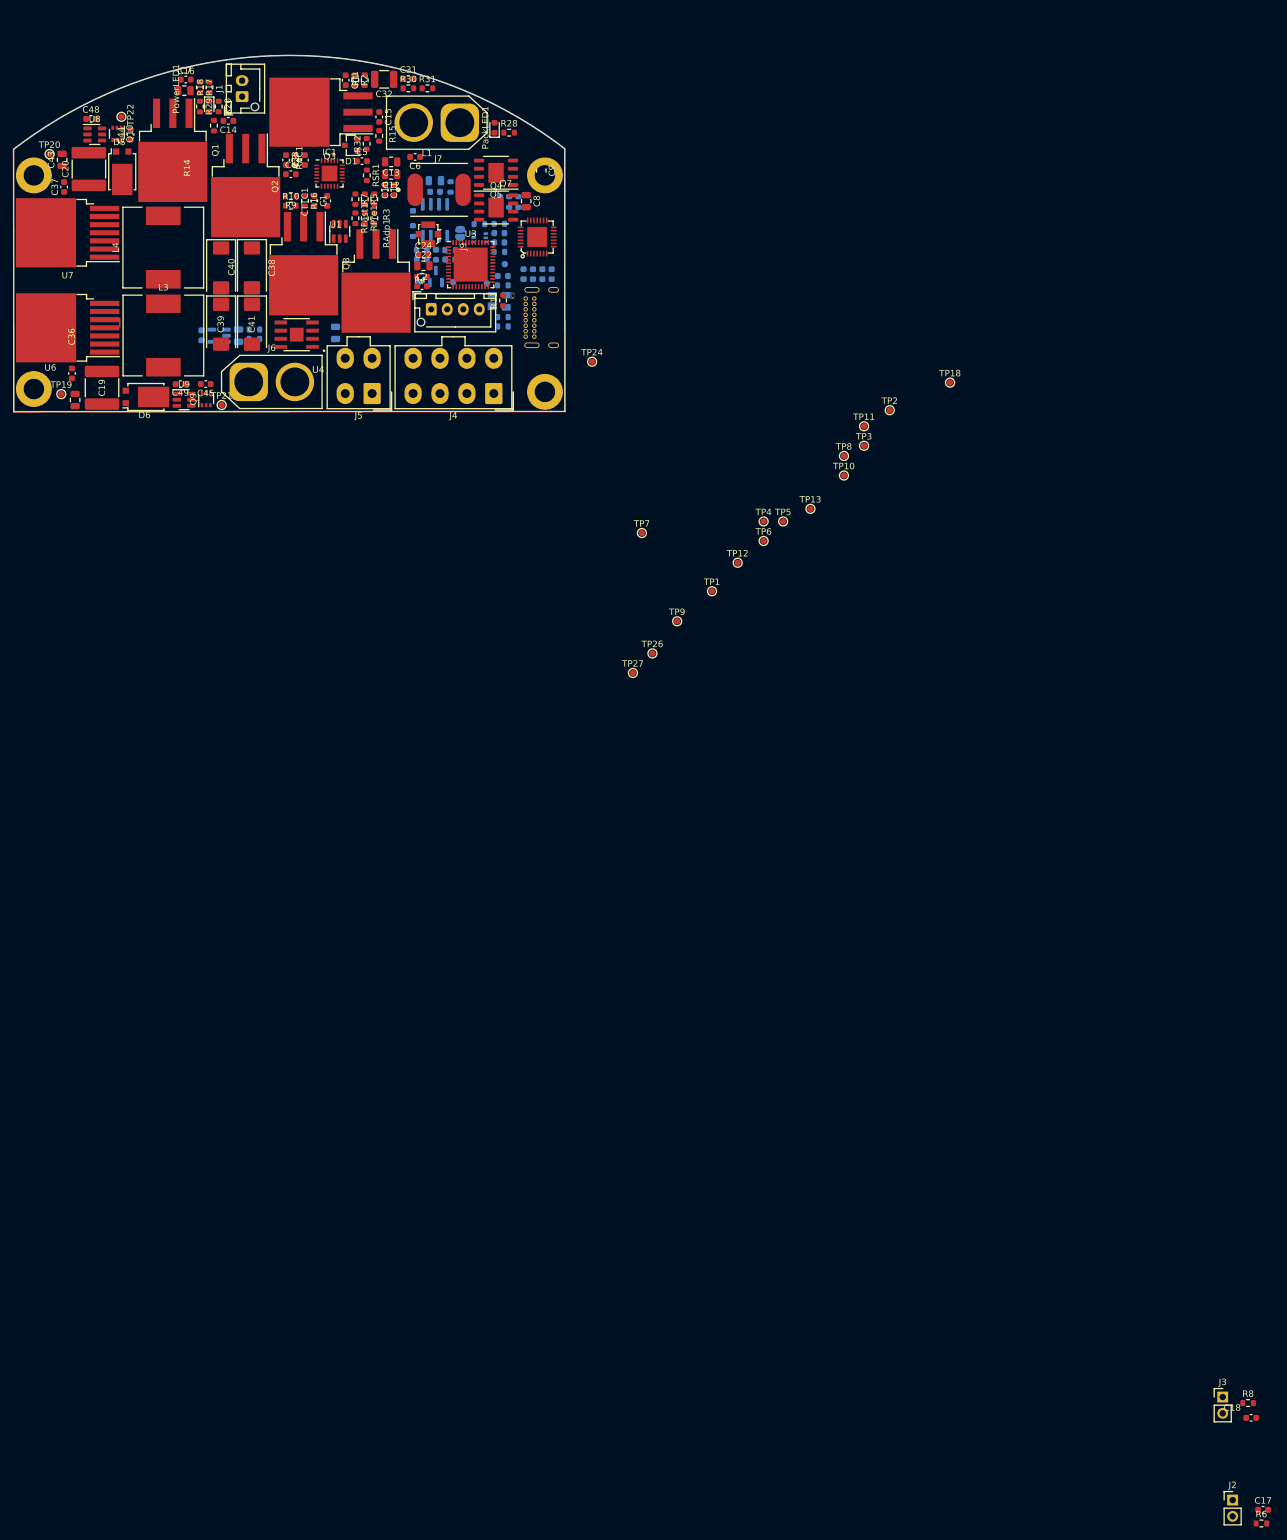
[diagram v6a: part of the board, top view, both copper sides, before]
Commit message: changed isolation switch position
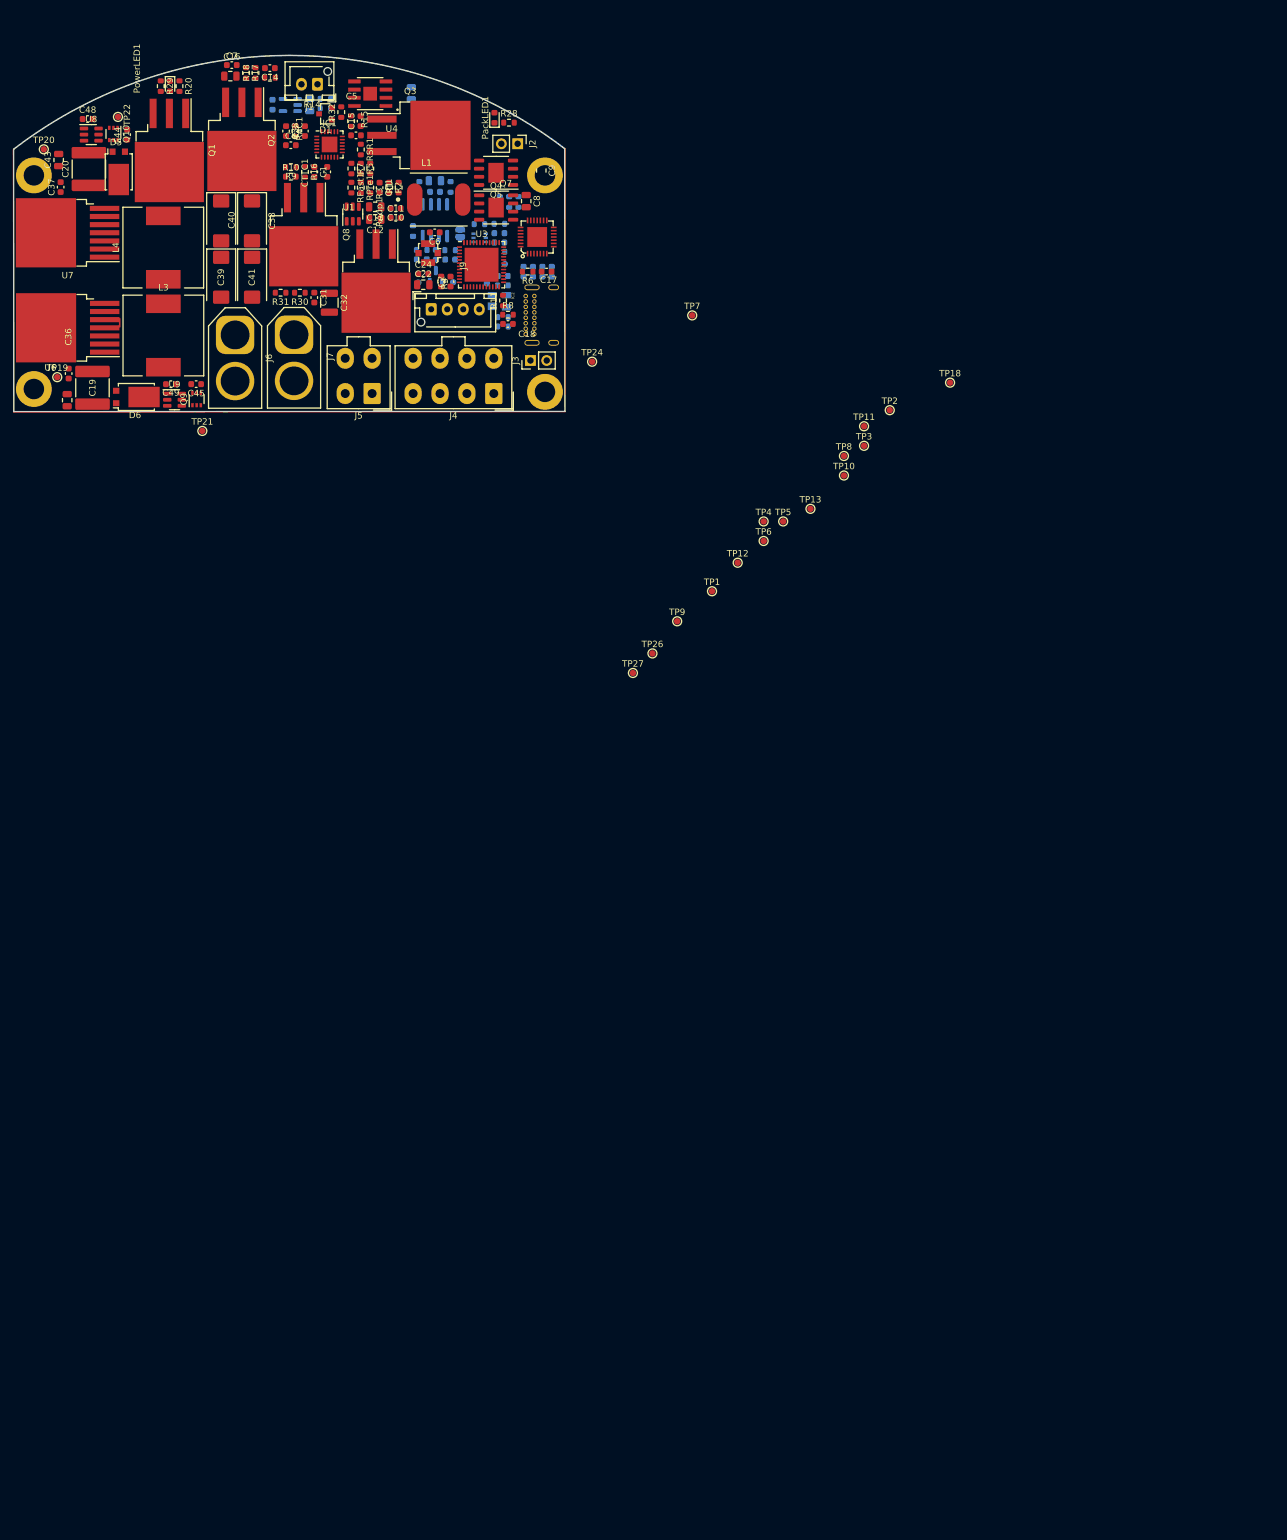
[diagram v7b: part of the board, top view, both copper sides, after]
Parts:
- moved J2 239.4 mm to (127.6, 41.2), turned to -90 degrees
- moved R6 226.6 mm to (129.2, 61.1), turned to 180 degrees
- moved C17 223.4 mm to (132.2, 61.1), turned to 180 degrees
- moved C18 206.5 mm to (126.1, 69.3), turned to 180 degrees
- moved R8 205.5 mm to (126.1, 67.8)
- moved J3 194.6 mm to (129.6, 75.0), turned to 90 degrees
- moved J7 42.0 mm to (92.7, 71.0), turned to -90 degrees
- moved U4 39.3 mm to (104.6, 33.3)
- moved R31 39.3 mm to (90.6, 64.4), turned to 180 degrees
- moved C54 39.2 mm to (111.0, 33.3)
- moved C57 37.7 mm to (95.2, 35.1)
- moved C58 37.7 mm to (89.4, 35.1)
- moved R42 37.7 mm to (97.6, 34.2)
- moved R43 37.7 mm to (97.6, 35.6)
- moved U11 37.7 mm to (92.1, 35.1)
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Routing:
- net Net-(C31-Pad1): track 0.00 -> 2.03 mm
